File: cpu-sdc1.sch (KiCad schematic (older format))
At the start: 2 parts

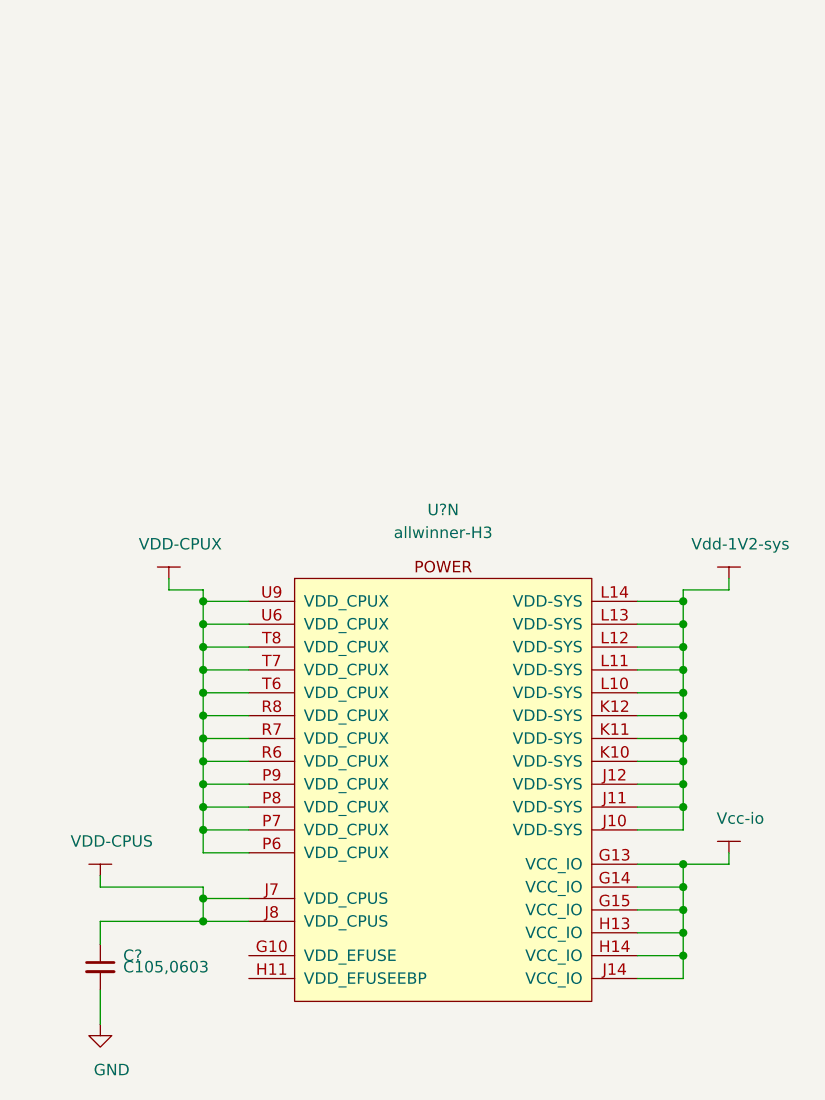
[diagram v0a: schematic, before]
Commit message: update cpu related schematic,
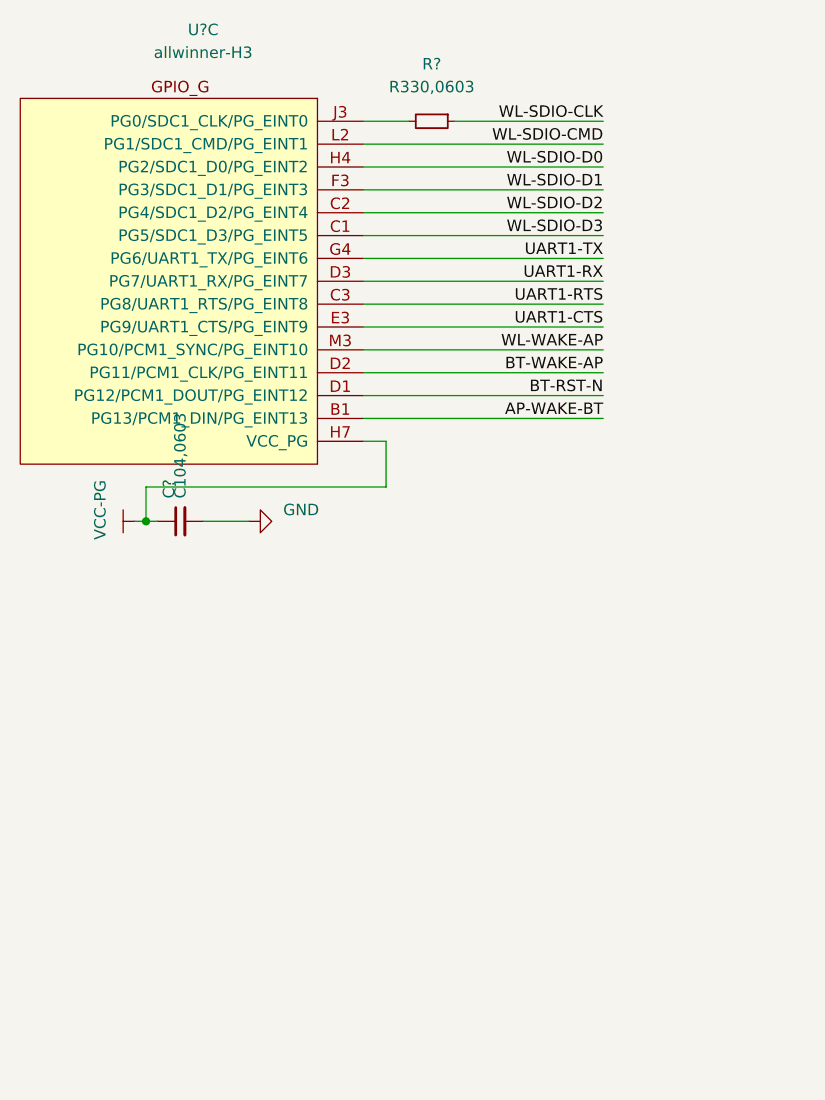
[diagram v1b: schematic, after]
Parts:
- removed C?: C105,0603, Capacitor_SMD:C_0603_1608Metric_Pad1.05x0.95mm_HandSolder, symbol taobao-c:C105,0603
- removed U?: allwinner-H3, symbol taobao-components:allwinner-H3
- added C?: C104,0603, Capacitor_SMD:C_0603_1608Metric_Pad1.05x0.95mm_HandSolder, symbol taobao-c:C104,0603
- added R?: R330,0603, Resistor_SMD:R_0603_1608Metric_Pad1.05x0.95mm_HandSolder, symbol taobao-r:R330,0603
- added U?: allwinner-H3, symbol taobao-components:allwinner-H3
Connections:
- net GND: now also C?.2
- new net: R?.2, U?.J3 (PG0/SDC1_CLK/PG_EINT0)
- new net AP-WAKE-BT: U?.B1 (PG13/PCM1_DIN/PG_EINT13)
- new net BT-RST-N: U?.D1 (PG12/PCM1_DOUT/PG_EINT12)
- new net BT-WAKE-AP: U?.D2 (PG11/PCM1_CLK/PG_EINT11)
- new net UART1-CTS: U?.E3 (PG9/UART1_CTS/PG_EINT9)
- new net UART1-RTS: U?.C3 (PG8/UART1_RTS/PG_EINT8)
- new net UART1-RX: U?.D3 (PG7/UART1_RX/PG_EINT7)
- new net UART1-TX: U?.G4 (PG6/UART1_TX/PG_EINT6)
- new net VCC-PG: C?.1, U?.H7 (VCC_PG)
- new net WL-SDIO-CLK: R?.1
- new net WL-SDIO-CMD: U?.L2 (PG1/SDC1_CMD/PG_EINT1)
- new net WL-SDIO-D0: U?.H4 (PG2/SDC1_D0/PG_EINT2)
- new net WL-SDIO-D1: U?.F3 (PG3/SDC1_D1/PG_EINT3)
- new net WL-SDIO-D2: U?.C2 (PG4/SDC1_D2/PG_EINT4)
- new net WL-SDIO-D3: U?.C1 (PG5/SDC1_D3/PG_EINT5)
- new net WL-WAKE-AP: U?.M3 (PG10/PCM1_SYNC/PG_EINT10)
